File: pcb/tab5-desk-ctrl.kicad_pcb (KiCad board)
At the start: 2 copper layers, 60 x 35.2 mm, 18 parts, among them U1A Socket 1x15 2.54mm, U1B Socket 1x15 2.54mm

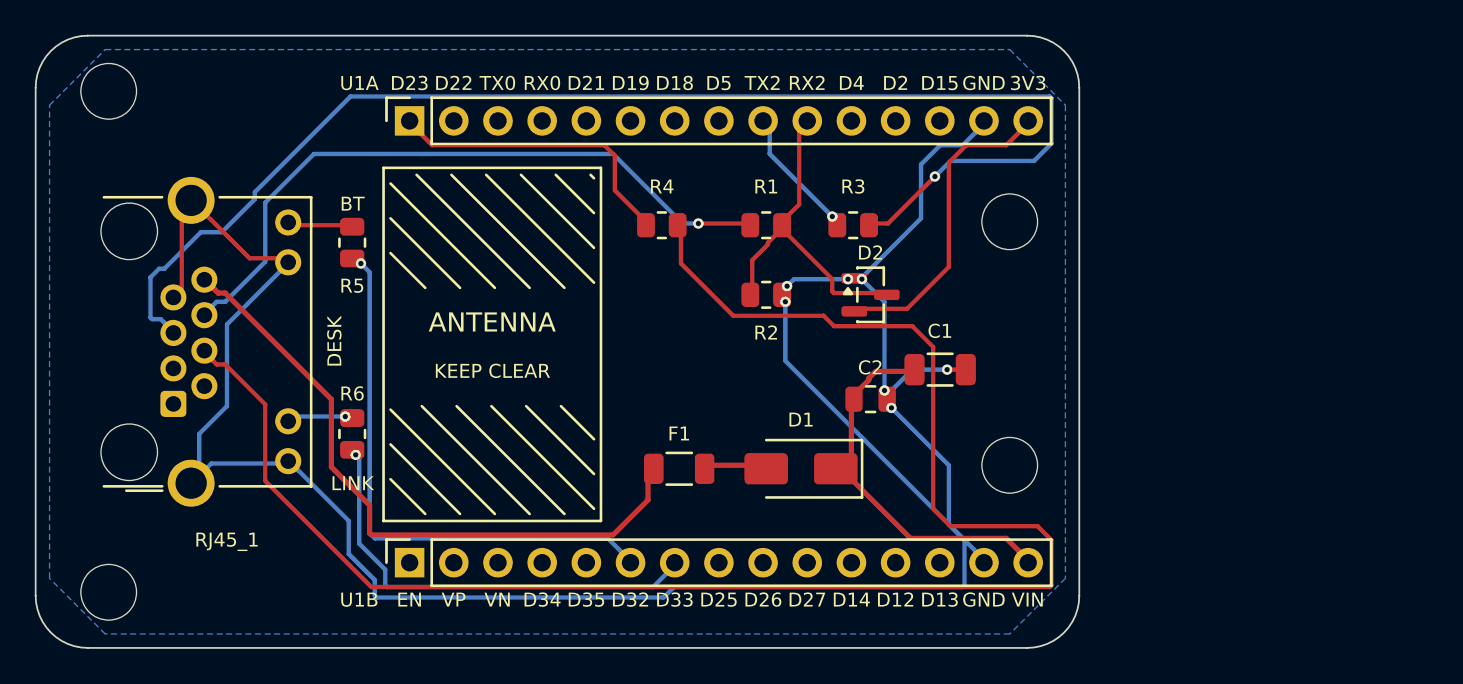
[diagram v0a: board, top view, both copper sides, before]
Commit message: The companion's carrier board rev2: pins 5 and 6 the way the box uses them, the divider on pin 5 where it sends and the 220R on pin 6 where it listens, as the published tables have it; the DevKit 10 mm further from the jack, and in the room that frees the 5 V input with a 1000 uF electrolytic for the radio's start-up surge, which browned rev1 out on desk power alone; thermal reliefs on the ground pads, with the router keeping other nets off the jack's pin 7; the jack's pin numbers and what each carries on the back; the README, the wiring figure and the companion's defaults to match
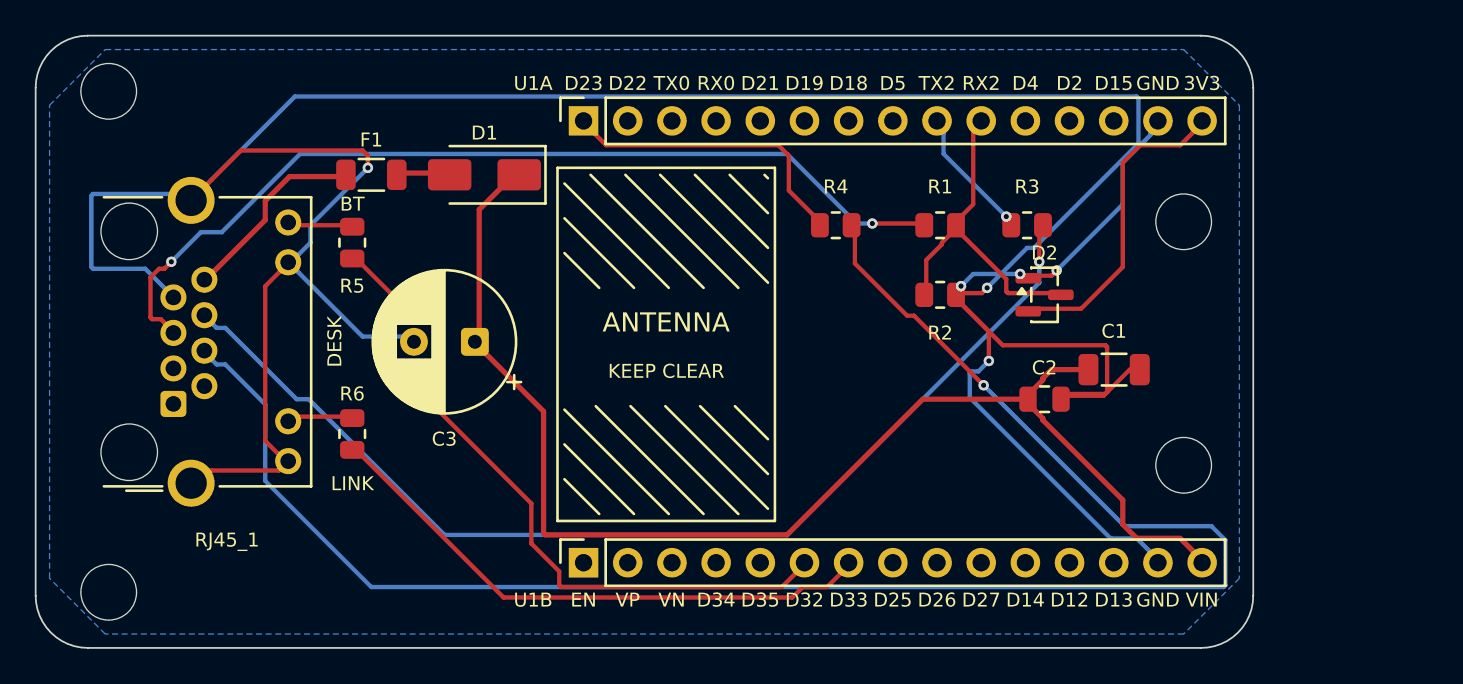
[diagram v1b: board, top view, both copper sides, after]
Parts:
- added C3: 1000uF 6.3V, Capacitor_THT:CP_Radial_D8.0mm_P3.50mm, F.Cu at (25.2, 17.6)
- moved D1 24.8 mm to (25.8, 8.00)
- moved F1 24.5 mm to (19.3, 8.00)
- moved C1 10.0 mm to (62.0, 19.2)
- moved C2 10.0 mm to (58.0, 20.9)
- moved D2 10.0 mm to (58.0, 14.9)
- moved H3 10.0 mm to (66.0, 10.7)
- moved H4 10.0 mm to (66.0, 24.7)
- moved R1 10.0 mm to (52.0, 10.9)
- moved R2 10.0 mm to (52.0, 14.9)
- moved R3 10.0 mm to (57.0, 10.9)
- moved R4 10.0 mm to (46.0, 10.9)
- moved U1A 10.0 mm to (31.5, 4.90)
- moved U1B 10.0 mm to (31.5, 30.3)
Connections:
- RJ45_1 pad 5: DESK_RX -> DESK_TX
- RJ45_1 pad 6: DESK_TX -> DESK_RX
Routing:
- net GND: track 142.6 -> 196.6 mm, vias 7 -> 6
- net +5V: track 22.0 -> 73.7 mm
- net DESK_5V: track 37.5 -> 11.2 mm
- net DESK_TX: track 38.9 -> 53.1 mm, vias 1 -> 2
- net DESK_RX: track 75.4 -> 62.6 mm
- net LED_DESK: track 25.9 -> 32.9 mm, vias 1 -> 0
- net LED_BT: track 32.0 -> 38.6 mm, vias 1 -> 0
- net PIN20: track 95.1 -> 99.7 mm, vias 0 -> 1
- net D5V_F: track 3.61 -> 3.06 mm
- net LED_DESK_A: vias 1 -> 0
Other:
- board size 60 x 35.2 mm -> 70 x 35.2 mm
- board text added: "1"
- board text added: "2"
- board text added: "3"
- board text added: "4"
- board text added: "4 wake"
- board text added: "5"
- board text added: "6"
- board text added: "6 box RX 5 box TX"
- board text added: "7"
- board text added: "8"
- board text added: "8 5V 7 GND"
- board text added: "rev2"
- board text removed: "rev1"

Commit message: The rev2 board 10 mm longer again, so the DevKit stays clear of C3 however far it reaches past its first pin; the DevKit's pin names, BT, LINK and C3's + on the back as well, where the probe goes; the schematic redrawn: left to right from the jack to the module, power as named symbols instead of labels, every field level, no pin numbers on two-pin parts, each label at the end of its stub, C3 in the 5 V input and the new mounting pattern; check_sch.py reads a field's justification and its symbol's turn
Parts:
- moved C1 10.0 mm to (72.0, 19.2)
- moved C2 10.0 mm to (68.0, 20.9)
- moved D2 10.0 mm to (68.0, 14.9)
- moved H3 10.0 mm to (76.0, 10.7)
- moved H4 10.0 mm to (76.0, 24.7)
- moved R1 10.0 mm to (62.0, 10.9)
- moved R2 10.0 mm to (62.0, 14.9)
- moved R3 10.0 mm to (67.0, 10.9)
- moved R4 10.0 mm to (56.0, 10.9)
- moved U1A 10.0 mm to (41.5, 4.90)
- moved U1B 10.0 mm to (41.5, 30.3)
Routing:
- net LED_DESK: track 32.9 -> 42.9 mm
- net GND: track 196.6 -> 206.6 mm
- net DESK_RX: track 62.6 -> 72.6 mm
- net PIN20: track 99.7 -> 109.7 mm
- net DESK_TX: track 53.1 -> 63.1 mm
- net LED_BT: track 38.6 -> 45.3 mm
- net +5V: track 73.7 -> 79.7 mm
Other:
- board size 70 x 35.2 mm -> 80 x 35.2 mm
- board text added: "+"

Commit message: The rev2 schematic on A5 and packed: plain net labels written over their stubs, the board's signal nets named as KiCad names them on the root sheet so parity holds, the LEDs beside the jack, and notes with the box's pinout, the readings to expect at idle, the GPIOs, what the LEDs say and which way C3 goes; LED nets named BT and LINK as on the silkscreen; C3 470 uF 10 V, and optional
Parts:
- C3: value 1000uF 6.3V -> 470uF 10V
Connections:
- net D5V_F renamed /D5V_F
- net DESK_5V renamed /DESK_5V
- net DESK_RX renamed /DESK_RX
- net DESK_TX renamed /DESK_TX
- net ESP_P20 renamed /ESP_P20
- net ESP_TX renamed /ESP_TX
- net LED_BT renamed /BT_LED
- net LED_BT_A renamed /BT_A
- net LED_DESK renamed /LINK_LED
- net LED_DESK_A renamed /LINK_A
- net PIN20 renamed /PIN20
- net RX_DIV renamed /RX_DIV
